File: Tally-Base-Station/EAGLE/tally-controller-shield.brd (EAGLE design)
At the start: 101.6 x 53.6 mm, 24 parts, among them J2 Mega R3, U1 SN75174N, U2 SN75174N, U3 SN75174N

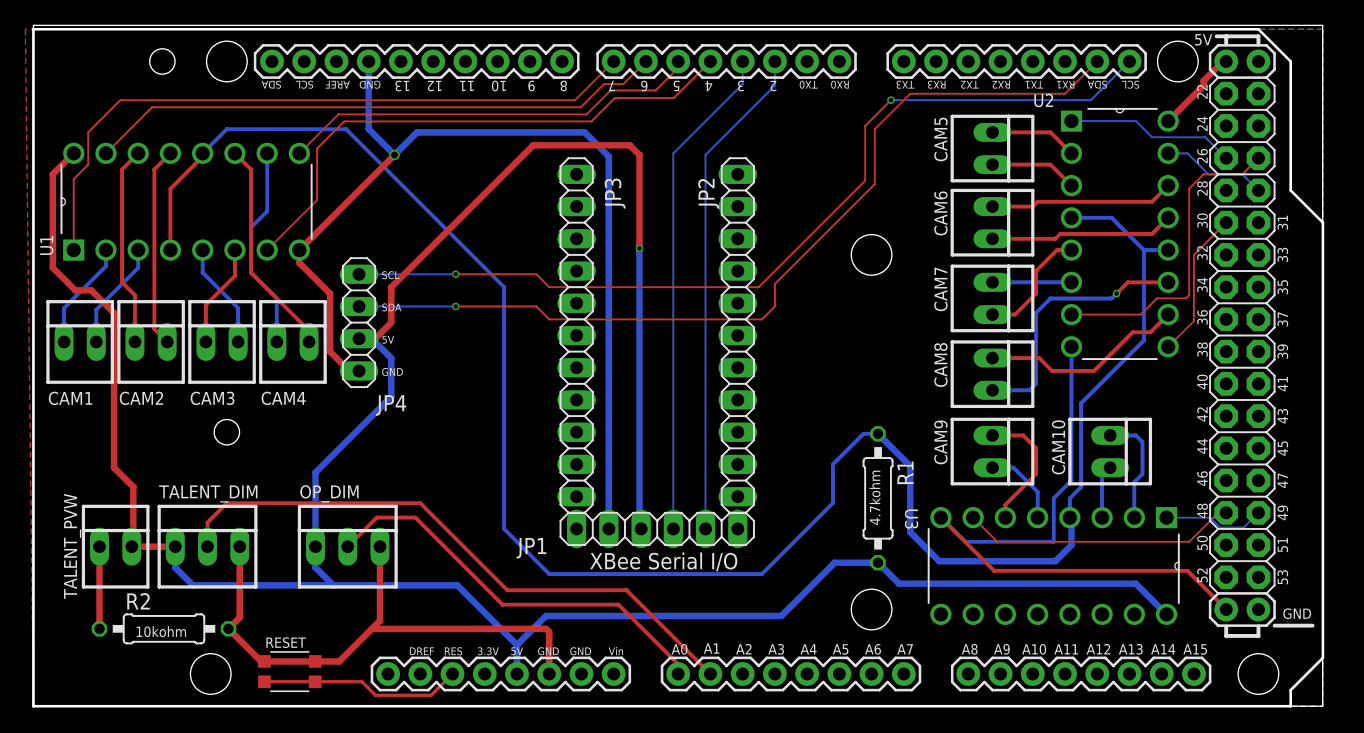
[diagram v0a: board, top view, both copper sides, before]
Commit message: Add some additional headers, fix switch wiring.
Add extra I2C connector that will work with a right-angle header.
Add a neopixel header for a possible system status light.
Wire switch to input (missed that in the schematic)
Trim the number of headers for holding the XBee regulated breakout to make routing easier
Add a bunch of labels to things on the top silkscreen.
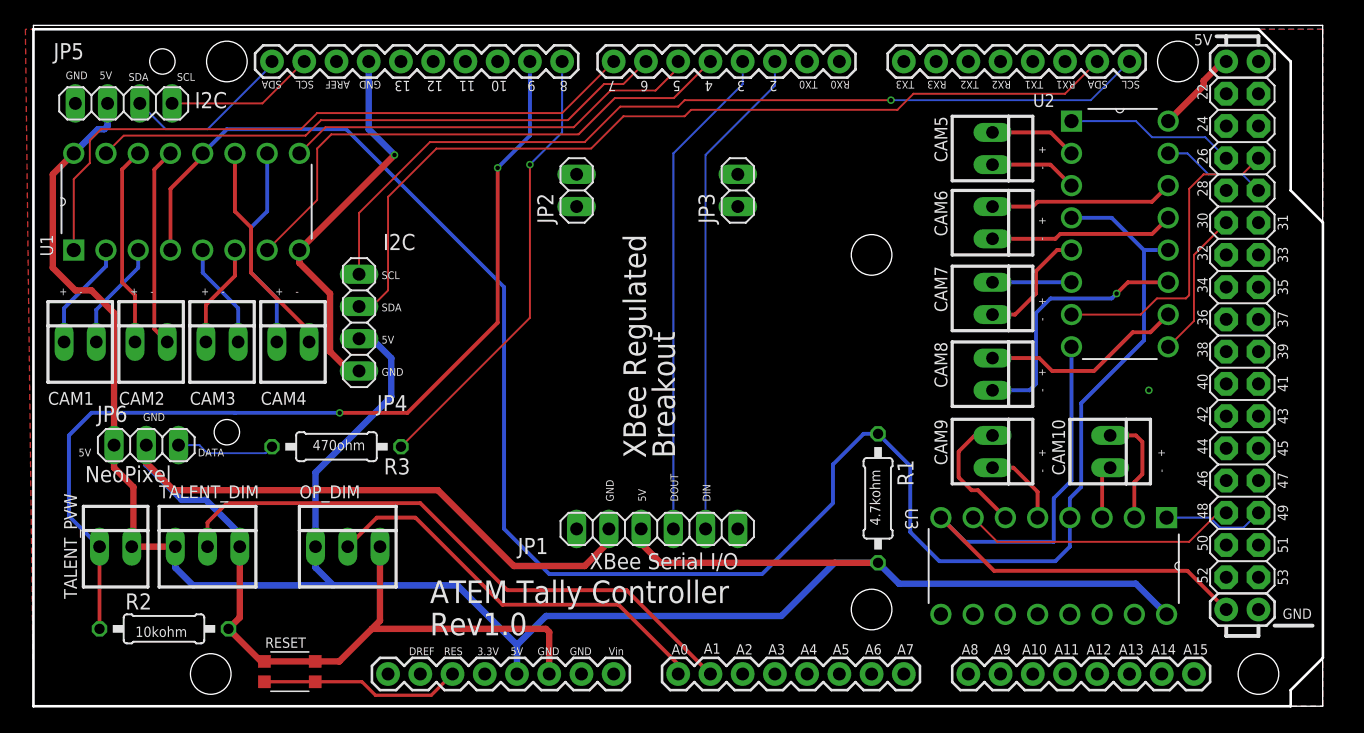
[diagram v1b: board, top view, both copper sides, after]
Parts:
- added JP5: I2C, pinhead:1X04
- added JP6: NeoPixel, pinhead:1X03
- added R3: 470ohm, rcl:0207/10
- JP2, JP3: device pinhead:1X11 -> pinhead:1X02
- moved JP2 17.1 mm to (42.8, 40.6)
- moved JP3 17.1 mm to (55.5, 40.6)
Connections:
- removed net N$1: R2.1, TALENT_PVW.1
- new net NEOPIXELDATA: JP6.3, R3.2
- net 5V@0: now also JP5.2, JP6.1
- net GND: now also JP5.1, JP6.2
- net MEGA8: now also R3.1
- net MEGA9: now also R2.1, TALENT_PVW.1
- net MEGASCL1: now also JP5.4
- net MEGASDA1: now also JP5.3
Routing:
- net MEGA9: track 0.00 -> 75.3 mm, vias 0 -> 2
- net MEGA8: track 0.00 -> 35.6 mm, vias 0 -> 1
- net 5V@0: track 211.5 -> 177.4 mm, vias 1 -> 0
- net MEGASDA1: track 0.00 -> 13.6 mm
- net MEGASCL1: track 0.00 -> 11.8 mm
- net NEOPIXELDATA: track 0.00 -> 7.84 mm
- net GND: track 174.0 -> 181.4 mm, vias 1 -> 2
- net N$1: track 6.48 -> 0.00 mm
- net MEGASCL: track 71.0 -> 70.5 mm, vias 2 -> 1
- net MEGASDA: track 70.6 -> 70.5 mm, vias 1 -> 0
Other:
- board text added: "+ -"
- board text added: "- +"
- board text added: "ATEM Tally Controller"
- board text added: "Breakout"
- board text added: "DATA"
- board text added: "DIN"
- board text added: "DOUT"
- board text added: "XBee Regulated"
- board text removed: "ATEM Camera Tally Controller"

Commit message: Major rework of the shield to make a much better layout.
- Expanded to 12 camera support out of the box
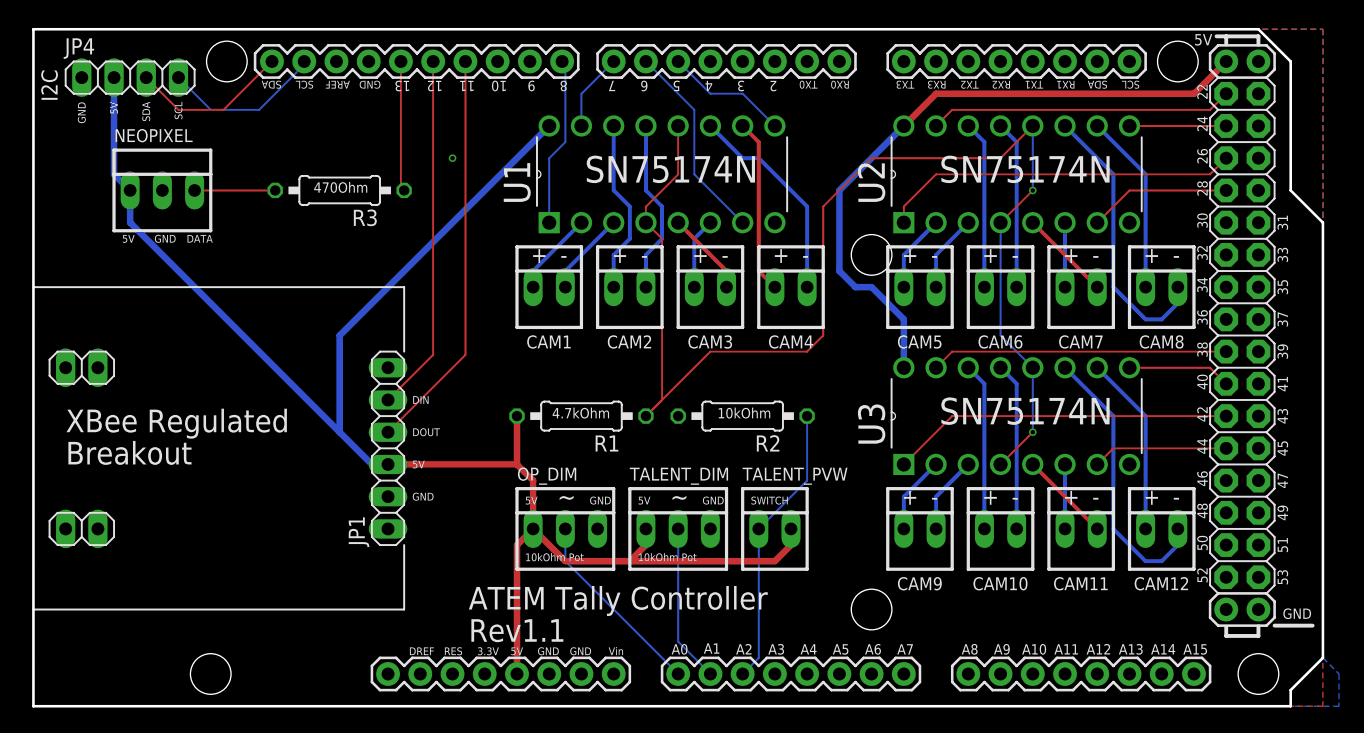
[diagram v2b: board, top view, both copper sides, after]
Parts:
- removed JP5: I2C, pinhead:1X04
- removed JP6: NeoPixel, pinhead:1X03
- removed S1: KMR2, zortness:TACTILE_KMR2
- added CAM11, CAM12: 22-23-2021, con-molex:22-23-2021
- added NEOPIXEL: 22-23-2031, con-molex:22-23-2031
- R1: value 4.7kohm -> 4.7kOhm
- R2: value 10kohm -> 10kOhm
- R3: value 470ohm -> 470Ohm
- moved JP3 58.2 mm to (3.81, 14.0), turned to 0 degrees
- moved TALENT_PVW 52.0 mm to (58.4, 14.0)
- moved R2 48.6 mm to (55.9, 22.9), turned to 180 degrees
- moved JP2 41.4 mm to (3.81, 26.7), turned to 0 degrees
- moved CAM4 39.5 mm to (59.7, 33.0)
- moved CAM3 38.7 mm to (53.3, 33.0)
- moved CAM2 38.0 mm to (47.0, 33.0)
- moved U1 37.5 mm to (58.4, 45.7)
- moved CAM1 37.2 mm to (40.6, 33.0)
- moved TALENT_DIM 37.1 mm to (50.8, 14.0)
- moved JP4 26.4 mm to (7.62, 49.5), turned to 0 degrees
- moved U3 24.5 mm to (86.4, 26.7), turned to 90 degrees
- moved R1 24.2 mm to (43.2, 22.9), turned to 180 degrees
- moved JP1 22.1 mm to (27.9, 20.3), turned to 90 degrees
- moved R3 20.2 mm to (24.1, 40.6)
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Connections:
- new net CAM11D+: CAM11.1, U3.6
- new net CAM11D-: CAM11.2, U3.5
- new net CAM12D+: CAM12.1, U3.10
- new net CAM12D-: CAM12.2, U3.11
- net 5V@0: now also NEOPIXEL.1; no longer JP5.2, JP6.1, U3.16
- net 5V@1: now also U3.16
- net CAM10D+: now also U3.14; no longer U3.2
- net CAM10D-: now also U3.13; no longer U3.3
- net CAM9D+: now also U3.2; no longer U3.6
- net CAM9D-: now also U3.3; no longer U3.5
- net GND: now also NEOPIXEL.2; no longer JP5.1, JP6.2, S1.3, S1.4
- net MEGA11: now also JP1.4
- net MEGA12: now also JP1.5
- net MEGA13: now also R3.1
- net MEGA2: no longer JP1.5
- net MEGA22: now also U2.15
- net MEGA24: now also U2.9
- net MEGA27: no longer U2.7
- net MEGA28: now also U2.7
- net MEGA29: no longer U2.15
- net MEGA3: no longer JP1.4
- net MEGA30: no longer U2.9
- net MEGA38: now also U3.15
- net MEGA4: no longer U1.7
- net MEGA40: now also U3.9
- net MEGA42: now also U3.1
- net MEGA44: now also U3.7
- net MEGA48: no longer U3.7
- net MEGA49: no longer U3.1
- net MEGA6: now also U1.7; no longer U1.15
- net MEGA7: now also U1.15; no longer U1.1
- net MEGA8: now also U1.1; no longer R3.1
- net MEGA9: no longer R2.1, TALENT_PVW.1
- net MEGAA2: now also R2.1, TALENT_PVW.1
- net MEGASCL: no longer JP4.4
- net MEGASCL1: now also JP4.4; no longer JP5.4
- net MEGASDA: no longer JP4.3
- net MEGASDA1: now also JP4.3; no longer JP5.3
- net NEOPIXELDATA: now also NEOPIXEL.3; no longer JP6.3
- net RESET: no longer S1.1, S1.2
- net RS485EN: now also U3.12
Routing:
- net GND: track 181.4 -> 0.00 mm, vias 2 -> 1
- net MEGA9: track 75.3 -> 0.00 mm, vias 2 -> 0
- net MEGASDA: track 70.5 -> 0.00 mm
- net MEGASCL: track 70.5 -> 0.00 mm, vias 1 -> 0
- net RS485EN: track 152.0 -> 100.7 mm, vias 0 -> 2
- net 5V@0: track 177.4 -> 128.9 mm
- net MEGA7: track 53.0 -> 6.13 mm
- net 5V@1: track 6.74 -> 51.5 mm
- net MEGA4: track 43.5 -> 0.00 mm
- net MEGA3: track 39.1 -> 0.00 mm
- net MEGA2: track 39.1 -> 0.00 mm
- net MEGAA1: track 47.7 -> 12.5 mm
- net MEGA11: track 0.00 -> 31.7 mm
- net MEGA6: track 45.5 -> 15.9 mm
- net MEGA12: track 0.00 -> 28.1 mm
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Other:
- board size 101.6 x 53.6 mm -> 101.6 x 53.3 mm
- board text added: "10kOhm Pot"
- board text added: "Rev1.1"
- board text added: "SWITCH"
- board text added: "~"
- board text removed: "- +"
- board text removed: "RESET"
- board text removed: "Rev1.0"

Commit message: Standardize RS485 pinouts, update RJ45 pinouts.
Fix pin assignments for the RS485 interconnects to standardize on pin1 = data-.
Update the RJ45 breakouts to be mostly pin compatible with DMX over ethernet wiring standard (using pin 5/6 for V+)
Create an XLR RS485 breakout option for wiring cameras together using 3pin DMX cables
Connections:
- net 5V@0: now also NEOPIXEL.2, OP_DIM.3, TALENT_DIM.3; no longer NEOPIXEL.1, OP_DIM.1, TALENT_DIM.1
- net CAM10D+: now also CAM10.2; no longer CAM10.1
- net CAM10D-: now also CAM10.1; no longer CAM10.2
- net CAM11D+: now also CAM11.2; no longer CAM11.1
- net CAM11D-: now also CAM11.1; no longer CAM11.2
- net CAM12D+: now also CAM12.2; no longer CAM12.1
- net CAM12D-: now also CAM12.1; no longer CAM12.2
- net CAM1D+: now also CAM1.2; no longer CAM1.1
- net CAM1D-: now also CAM1.1; no longer CAM1.2
- net CAM2D+: now also CAM2.2; no longer CAM2.1
- net CAM2D-: now also CAM2.1; no longer CAM2.2
- net CAM3D+: now also CAM3.2; no longer CAM3.1
- net CAM3D-: now also CAM3.1; no longer CAM3.2
- net CAM4D+: now also CAM4.2; no longer CAM4.1
- net CAM4D-: now also CAM4.1; no longer CAM4.2
- net CAM5D+: now also CAM5.2; no longer CAM5.1
- net CAM5D-: now also CAM5.1; no longer CAM5.2
- net CAM6D+: now also CAM6.2; no longer CAM6.1
- net CAM6D-: now also CAM6.1; no longer CAM6.2
- net CAM7D+: now also CAM7.2; no longer CAM7.1
- net CAM7D-: now also CAM7.1; no longer CAM7.2
- net CAM8D+: now also CAM8.2; no longer CAM8.1
- net CAM8D-: now also CAM8.1; no longer CAM8.2
- net CAM9D+: now also CAM9.2; no longer CAM9.1
- net CAM9D-: now also CAM9.1; no longer CAM9.2
- net GND: now also NEOPIXEL.1, OP_DIM.1, TALENT_DIM.1; no longer NEOPIXEL.2, OP_DIM.3, TALENT_DIM.3
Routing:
- net CAM8D-: track 22.2 -> 15.3 mm
- net CAM12D-: track 22.2 -> 15.3 mm
- net CAM1D-: track 6.66 -> 9.20 mm
- net CAM9D-: track 6.13 -> 7.93 mm
- net CAM5D-: track 6.13 -> 7.93 mm
- net CAM4D-: track 16.6 -> 14.8 mm
- net CAM9D+: track 6.13 -> 5.08 mm
- net CAM8D+: track 14.3 -> 15.3 mm
- net CAM5D+: track 6.13 -> 5.08 mm
- net CAM12D+: track 14.3 -> 15.3 mm
- net CAM3D-: track 6.66 -> 5.61 mm
- net CAM1D+: track 6.66 -> 5.61 mm
- net CAM4D+: track 13.8 -> 14.8 mm
- net CAM7D-: track 7.18 -> 6.13 mm
- net CAM7D+: track 5.08 -> 6.13 mm
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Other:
- board text added: "- +"
- board text removed: "+ -"

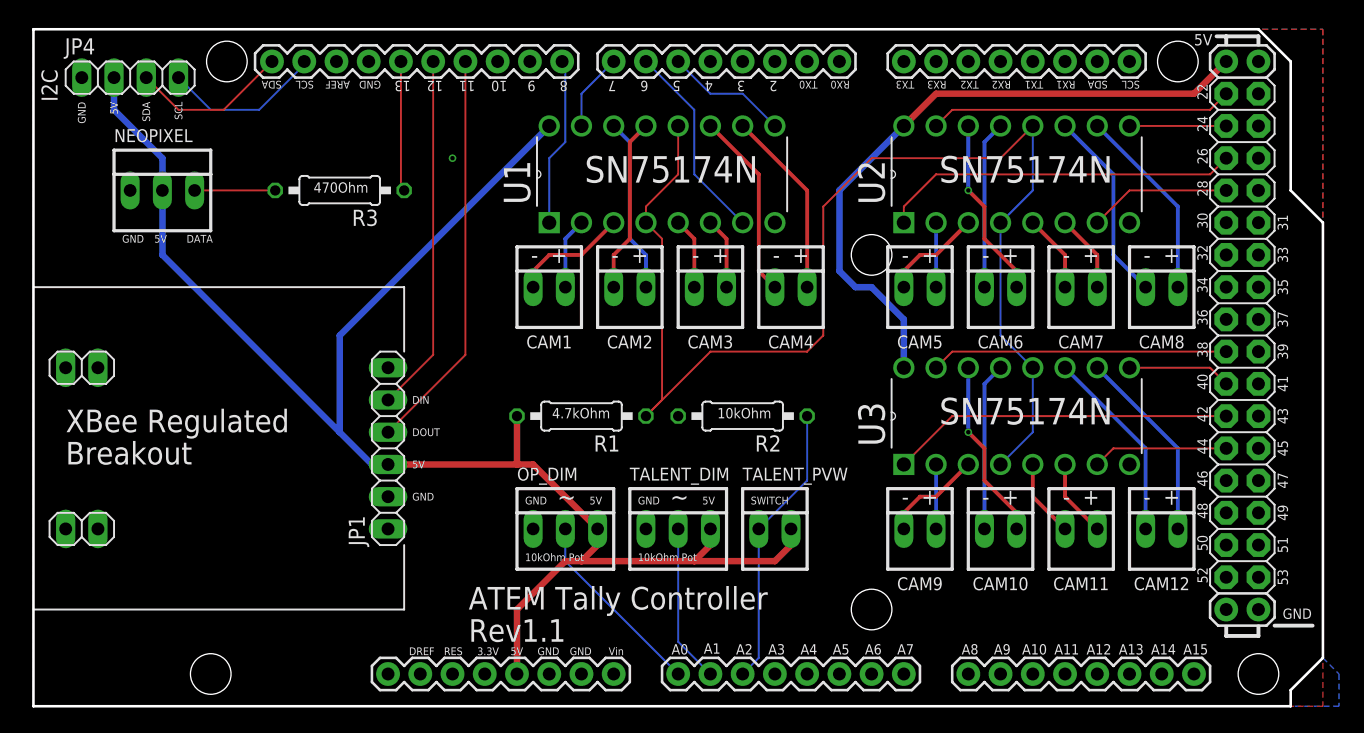
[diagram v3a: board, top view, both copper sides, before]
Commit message: Re-arrange components on controller shield to interfere less with the ethernet jack.
Creat a quick power distro for the output boards.
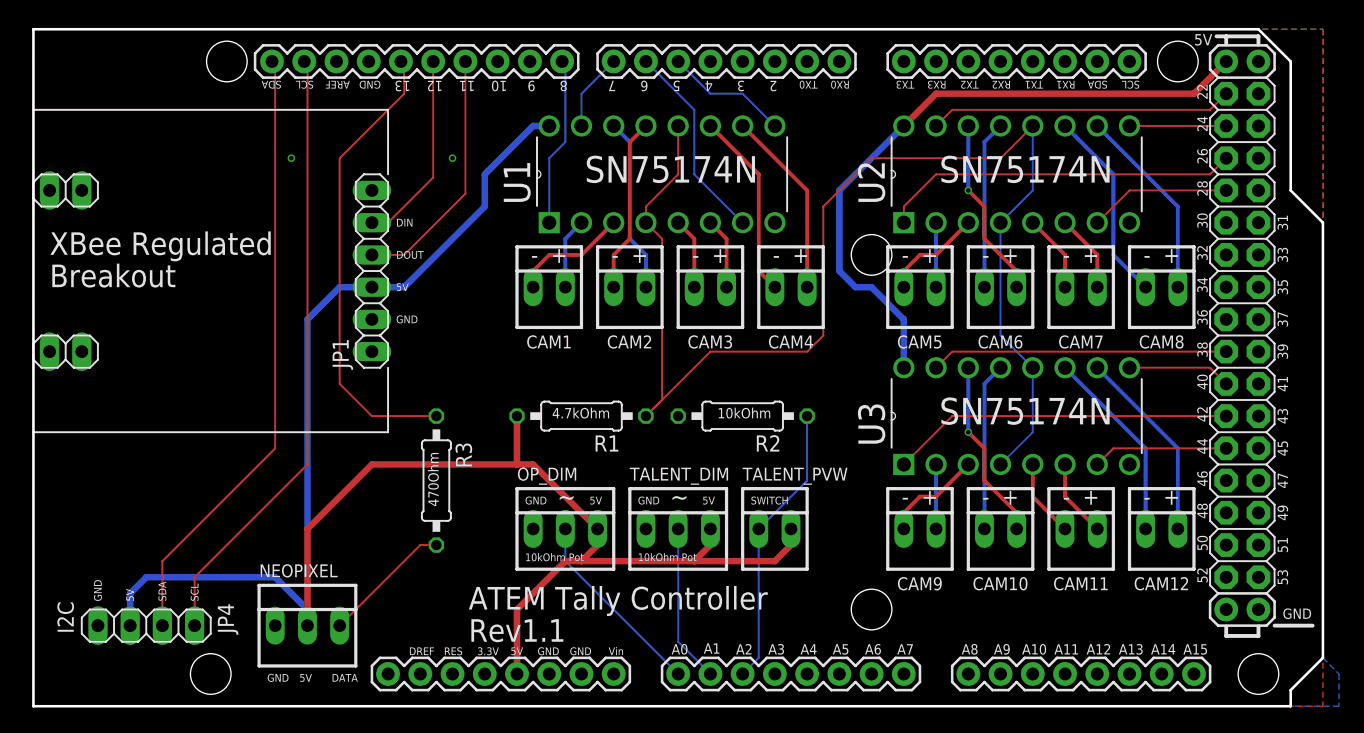
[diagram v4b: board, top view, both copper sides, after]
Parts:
- moved JP4 43.2 mm to (8.89, 6.35)
- moved NEOPIXEL 36.1 mm to (21.6, 6.35)
- moved R3 24.1 mm to (31.8, 17.8), turned to 270 degrees
- moved JP3 14.0 mm to (2.54, 27.9)
- moved JP1 14.0 mm to (26.7, 34.3)
- moved JP2 14.0 mm to (2.54, 40.6)
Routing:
- net MEGASDA1: track 12.5 -> 48.2 mm
- net MEGASCL1: track 12.7 -> 48.2 mm
- net MEGA13: track 10.3 -> 36.3 mm
- net 5V@0: track 129.7 -> 143.7 mm
- net MEGA12: track 28.1 -> 15.4 mm
- net MEGA11: track 31.7 -> 19.8 mm
- net NEOPIXELDATA: track 6.35 -> 10.3 mm
